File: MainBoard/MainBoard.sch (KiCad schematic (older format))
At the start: 6 parts

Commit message: add hierachy pins
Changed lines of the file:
@@
 F0 "keyboard" 50
 F1 "keyboard.sch" 50
+F2 "USB_D+" B R 10700 12500 50
+F3 "USB_D-" B R 10700 12700 50
 $EndSheet
 $EndSCHEMATC

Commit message: add hierachy pins
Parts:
- removed J?: Conn_Coaxial, symbol Connector:Conn_Coaxial
- J?: value DF40C-100DS-0.4V(51) -> DF40C-100DS-0.4V(51) _LFT
- J?: value DF40C-100DS-0.4V(51) -> DF40C-100DS-0.4V(51) _RFT
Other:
- moved on the sheet: J?
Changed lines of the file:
@@
-$EndComp
-$Comp
-L Connector:Conn_Coaxial J?
-U 1 1 60395F77
-P 21200 7000
-F 0 "J?" H 21300 6975 50  0000 L CNN
-F 1 "Conn_Coaxial" H 21300 6884 50  0000 L CNN
-F 2 "" H 21200 7000 50  0001 C CNN
-F 3 " ~" H 21200 7000 50  0001 C CNN
-	1    21200 7000
-	1    0    0    -1
 $EndComp
 $Comp
@@
 P 4850 3750
 F 0 "J?" H 4850 6417 50  0000 C CNN
-F 1 "DF40C-100DS-0.4V(51)" H 4850 6326 50  0000 C CNN
+F 1 "DF40C-100DS-0.4V(51) _LFT" H 4850 6326 50  0000 C CNN
 F 2 "HRS_DF40C-100DS-0.4V(51)" H 4850 3750 50  0001 L BNN
 F 3 "" H 4850 3750 50  0001 L BNN
@@
 L DF40C-100DS-0.4V_51_:DF40C-100DS-0.4V(51) J?
 U 1 1 6039B9F7
-P 9300 3750
-F 0 "J?" H 9300 6417 50  0000 C CNN
-F 1 "DF40C-100DS-0.4V(51)" H 9300 6326 50  0000 C CNN
-F 2 "HRS_DF40C-100DS-0.4V(51)" H 9300 3750 50  0001 L BNN
-F 3 "" H 9300 3750 50  0001 L BNN
-F 4 "HRS" H 9300 3750 50  0001 L BNN "MF"
-F 5 "None" H 9300 3750 50  0001 L BNN "PACKAGE"
-F 6 "Good" H 9300 3750 50  0001 L BNN "AVAILABILITY"
-F 7 "$1.36 USD" H 9300 3750 50  0001 L BNN "PRICE"
-F 8 "DF40C-100DS-0.4V(51)" H 9300 3750 50  0001 L BNN "MP"
-	1    9300 3750
+P 8450 3750
+F 0 "J?" H 8450 6417 50  0000 C CNN
+F 1 "DF40C-100DS-0.4V(51) _RFT" H 8450 6326 50  0000 C CNN
+F 2 "HRS_DF40C-100DS-0.4V(51)" H 8450 3750 50  0001 L BNN
+F 3 "" H 8450 3750 50  0001 L BNN
+F 4 "HRS" H 8450 3750 50  0001 L BNN "MF"
+F 5 "None" H 8450 3750 50  0001 L BNN "PACKAGE"
+F 6 "Good" H 8450 3750 50  0001 L BNN "AVAILABILITY"
+F 7 "$1.36 USD" H 8450 3750 50  0001 L BNN "PRICE"
+F 8 "DF40C-100DS-0.4V(51)" H 8450 3750 50  0001 L BNN "MP"
+	1    8450 3750
 	1    0    0    -1
 $EndComp

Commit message: add some power stuff and an extra USB port
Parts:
- added BT? (x3): _, symbol Device:Battery_Cell
- added BT?: Battery Cell, symbol Device:Battery_Cell
- added C?: 10p, symbol Device:C_Small
- added J?: USB3_A, symbol Connector:USB3_A
- added R?: 1, symbol Device:R_Small_US
- added U?: LTC4055-1, Package_DFN_QFN:QFN-16-1EP_4x4mm_P0.65mm_EP2.15x2.15mm, symbol Battery_Management:LTC4055-1
- J?: value DF40C-100DS-0.4V(51) _RFT -> DF40C-100DS-0.4V(51) _RFT (PN + 100)
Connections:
- net labels added: GND
- wire segments 0 -> 30
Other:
- moved on the sheet: J?

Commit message: switch out battery IC for better charging current
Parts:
- removed C?: 10p, symbol Device:C_Small
- removed R?: 1, symbol Device:R_Small_US
- removed U?: LTC4055-1, Package_DFN_QFN:QFN-16-1EP_4x4mm_P0.65mm_EP2.15x2.15mm, symbol Battery_Management:LTC4055-1
- added J?: Barrel_Jack, symbol Connector:Barrel_Jack
- added U?: LTC4090EDJCPBF, DFN600X300X80-23N, symbol LTC4090EDJCPBF:LTC4090EDJCPBF
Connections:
- net labels added: +5V
- wire segments 30 -> 35
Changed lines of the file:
@@
 $EndComp
-$Comp
-L Battery_Management:LTC4055-1 U?
-U 1 1 6039541B
-P 17700 9350
-F 0 "U?" H 17700 10017 50  0000 C CNN
-F 1 "LTC4055-1" H 17700 9926 50  0000 C CNN
-F 2 "Package_DFN_QFN:QFN-16-1EP_4x4mm_P0.65mm_EP2.15x2.15mm" H 17700 8450 50  0001 C CNN
-F 3 "https://www.analog.com/media/en/technical-documentation/data-sheets/4055fb.pdf" H 17700 8850 50  0001 C CNN
-	1    17700 9350
-	-1   0    0    1
-$EndComp
-Wire Wire Line
-	17300 9350 17150 9350
-Wire Wire Line
-	17150 9350 17150 9150
-Wire Wire Line
-	17150 9150 17300 9150
-Wire Wire Line
-	18100 9650 18250 9650
-Wire Wire Line
-	18250 9650 18250 8650
-Wire Wire Line
-	18250 8650 17150 8650
-Wire Wire Line
-	17150 8650 17150 9150
-Connection ~ 17150 9150
 $Comp
 L Device:Battery_Cell BT?
@@
 	16750 8400 16450 8400
 Connection ~ 16450 8400
-Wire Wire Line
-	16450 8400 16300 8400
 Connection ~ 16150 8400
 Wire Wire Line
@@
 Wire Wire Line
 	16150 8100 16300 8100
-Wire Wire Line
-	16300 8400 16300 9550
-Wire Wire Line
-	16300 9550 17300 9550
-Connection ~ 16300 8400
-Wire Wire Line
-	16300 8400 16150 8400
 $Comp
 L power:GND #PWR?
@@
 	16300 8100 16450 8100
 $Comp
-L Device:R_Small_US R?
-U 1 1 603A333E
-P 18600 9650
-F 0 "R?" H 18668 9696 50  0000 L CNN
-F 1 "1" H 18668 9605 50  0000 L CNN
-F 2 "" H 18600 9650 50  0001 C CNN
-F 3 "~" H 18600 9650 50  0001 C CNN
-	1    18600 9650
-	-1   0    0    1
-$EndComp
-$Comp
-L Device:C_Small C?
-U 1 1 603A4DA4
-P 18600 9450
-F 0 "C?" H 18692 9496 50  0000 L CNN
-F 1 "10p" H 18692 9405 50  0000 L CNN
-F 2 "" H 18600 9450 50  0001 C CNN
-F 3 "~" H 18600 9450 50  0001 C CNN
-	1    18600 9450
-	-1   0    0    1
-$EndComp
-$Comp
-L power:GND #PWR?
-U 1 1 603A62A7
-P 18600 9350
-F 0 "#PWR?" H 18600 9100 50  0001 C CNN
-F 1 "GND" H 18605 9177 50  0000 C CNN
-F 2 "" H 18600 9350 50  0001 C CNN
-F 3 "" H 18600 9350 50  0001 C CNN
-	1    18600 9350
-	-1   0    0    1
-$EndComp
-Wire Wire Line
-	18600 9750 18100 9750
-Wire Wire Line
-	20250 10000 18600 10000
-Wire Wire Line
-	18600 10000 18600 9750
-Connection ~ 18600 9750
-$Comp
 L power:GND #PWR?
 U 1 1 603AA452
@@
 	-1   0    0    1
 $EndComp
+$Comp
+L power:+5V #PWR?
+U 1 1 603ABEB6
+P 4350 5150
+F 0 "#PWR?" H 4350 5000 50  0001 C CNN
+F 1 "+5V" V 4365 5278 50  0000 L CNN
+F 2 "" H 4350 5150 50  0001 C CNN
+F 3 "" H 4350 5150 50  0001 C CNN
+	1    4350 5150
+	0    -1   -1   0
+$EndComp
+$Comp
+L power:+5V #PWR?
+U 1 1 603AC889
+P 4350 5250
+F 0 "#PWR?" H 4350 5100 50  0001 C CNN
+F 1 "+5V" V 4365 5378 50  0000 L CNN
+F 2 "" H 4350 5250 50  0001 C CNN
+F 3 "" H 4350 5250 50  0001 C CNN
+	1    4350 5250
+	0    -1   -1   0
+$EndComp
+$Comp
+L power:+5V #PWR?
+U 1 1 603AD3CB
+P 4350 5350
+F 0 "#PWR?" H 4350 5200 50  0001 C CNN
+F 1 "+5V" V 4365 5478 50  0000 L CNN
+F 2 "" H 4350 5350 50  0001 C CNN
+F 3 "" H 4350 5350 50  0001 C CNN
+	1    4350 5350
+	0    -1   -1   0
+$EndComp
+$Comp
+L power:+5V #PWR?
+U 1 1 603AD3D1
+P 4350 5450
+F 0 "#PWR?" H 4350 5300 50  0001 C CNN
+F 1 "+5V" V 4365 5578 50  0000 L CNN
+F 2 "" H 4350 5450 50  0001 C CNN
+F 3 "" H 4350 5450 50  0001 C CNN
+	1    4350 5450
+	0    -1   -1   0
+$EndComp
+$Comp
+L power:+5V #PWR?
+U 1 1 603AE08F
+P 4350 5550
+F 0 "#PWR?" H 4350 5400 50  0001 C CNN
+F 1 "+5V" V 4365 5678 50  0000 L CNN
+F 2 "" H 4350 5550 50  0001 C CNN
+F 3 "" H 4350 5550 50  0001 C CNN
+	1    4350 5550
+	0    -1   -1   0
+$EndComp
+$Comp
+L power:+5V #PWR?
+U 1 1 603AE095
+P 4350 5650
+F 0 "#PWR?" H 4350 5500 50  0001 C CNN
+F 1 "+5V" V 4365 5778 50  0000 L CNN
+F 2 "" H 4350 5650 50  0001 C CNN
+F 3 "" H 4350 5650 50  0001 C CNN
+	1    4350 5650
+	0    -1   -1   0
+$EndComp
+Wire Wire Line
+	16150 8400 16300 8400
+$Comp
+L LTC4090EDJCPBF:LTC4090EDJCPBF U?
+U 1 1 603CC1BE
+P 18200 9500
+F 0 "U?" H 18200 10570 50  0000 C CNN
+F 1 "LTC4090EDJCPBF" H 18200 10479 50  0000 C CNN
+F 2 "DFN600X300X80-23N" H 18200 9500 50  0001 L BNN
+F 3 "" H 18200 9500 50  0001 L BNN
+F 4 "LTC4090EDJC#PBF" H 18200 9500 50  0001 L BNN "MPN"
+F 5 "56M8725" H 18200 9500 50  0001 L BNN "OC_NEWARK"
+F 6 "1663728" H 18200 9500 50  0001 L BNN "OC_FARNELL"
+F 7 "Linear Technology" H 18200 9500 50  0001 L BNN "SUPPLIER"
+F 8 "DFN-16" H 18200 9500 50  0001 L BNN "PACKAGE"
+	1    18200 9500
+	1    0    0    -1
+$EndComp
+$Comp
+L Connector:Barrel_Jack J?
+U 1 1 603CD806
+P 20800 10850
+F 0 "J?" H 20570 10808 50  0000 R CNN
+F 1 "Barrel_Jack" H 20570 10899 50  0000 R CNN
+F 2 "" H 20850 10810 50  0001 C CNN
+F 3 "~" H 20850 10810 50  0001 C CNN
+	1    20800 10850
+	-1   0    0    1
+$EndComp
+$Comp
+L power:GND #PWR?
+U 1 1 603CEDD1
+P 20500 10950
+F 0 "#PWR?" H 20500 10700 50  0001 C CNN
+F 1 "GND" H 20505 10777 50  0000 C CNN
+F 2 "" H 20500 10950 50  0001 C CNN
+F 3 "" H 20500 10950 50  0001 C CNN
+	1    20500 10950
+	1    0    0    -1
+$EndComp
+Wire Wire Line
+	17400 8800 16550 8800
+Wire Wire Line
+	16550 8800 16550 11400
+Wire Wire Line
+	16550 11400 19950 11400
+Wire Wire Line
+	19950 11400 19950 10750
+Wire Wire Line
+	19950 10750 20500 10750
+Wire Wire Line
+	19000 9000 19550 9000
+$Comp
+L power:+5V #PWR?
+U 1 1 603D2A2F
+P 19550 9000
+F 0 "#PWR?" H 19550 8850 50  0001 C CNN
+F 1 "+5V" V 19565 9128 50  0000 L CNN
+F 2 "" H 19550 9000 50  0001 C CNN
+F 3 "" H 19550 9000 50  0001 C CNN
+	1    19550 9000
+	0    1    1    0
+$EndComp
+Wire Wire Line
+	17400 8900 17000 8900
+Wire Wire Line
+	17000 8900 17000 8250
+Wire Wire Line
+	17000 8250 19900 8250
+Wire Wire Line
+	19900 8250 19900 10000
+Wire Wire Line
+	19900 10000 20250 10000
+Wire Wire Line
+	19000 9300 19850 9300
+Wire Wire Line
+	19850 9300 19850 8300
+Wire Wire Line
+	19850 8300 17050 8300
+Wire Wire Line
+	17050 8300 17050 8500
+Wire Wire Line
+	17050 8500 16300 8500
+Wire Wire Line
+	16300 8500 16300 8400
+Connection ~ 16300 8400
+Wire Wire Line
+	16300 8400 16450 8400
 $EndSCHEMATC

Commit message: add key matrix and assighn footprints
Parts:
- BT1, BT2, BT3, BT4: renamed from BT?; footprint (none) -> Connector_JST:JST_PH_S2B-PH-SM4-TB_1x02-1MP_P2.00mm_Horizontal
- J1, J2: renamed from J?; footprint HRS_DF40C-100DS-0.4V(51) -> Libs:HRS_DF40C-100DS-0.4V(51)
- J3: renamed from J?; footprint (none) -> Connector_HDMI:HDMI_A_Contact_Technology_HDMI-19APL2_Horizontal
- J4: renamed from J?; footprint (none) -> Connector_BarrelJack:BarrelJack_CUI_PJ-063AH_Horizontal
- J7: renamed from J?; footprint (none) -> Connector_USB:USB_C_Receptacle_Amphenol_12401548E4-2A
- U1: renamed from U?; footprint DFN600X300X80-23N -> Libs:DFN600X300X80-23N
- gave numbers to parts that had none: 2

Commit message: move power dilevery to a hierarchy sheet and wire HDMI1
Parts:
- removed BT1: Battery Cell, Connector_JST:JST_PH_S2B-PH-SM4-TB_1x02-1MP_P2.00mm_Horizontal, symbol Device:Battery_Cell
- removed BT2, BT3, BT4: _, Connector_JST:JST_PH_S2B-PH-SM4-TB_1x02-1MP_P2.00mm_Horizontal, symbol Device:Battery_Cell
- removed U1: LTC4090EDJCPBF, Libs:DFN600X300X80-23N, symbol LTC4090EDJCPBF:LTC4090EDJCPBF
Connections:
- net +5V: now also J3.18 (+5V)
- net GND: now also J3.11 (CKS), J3.17 (GND), J3.2 (D2S), J3.5 (D1S), J3.8 (D0S), J3.SH
- net at J3.1 (D2+): now also J2.46
- net at J3.10 (CK+): now also J2.64
- net at J3.12 (CK-): now also J2.66
- net at J3.13 (CEC): now also J2.49
- net at J3.15 (SCL): now also J2.47
- net at J3.16 (SDA): now also J2.45
- net at J3.19 (HPD): now also J2.43
- net at J3.3 (D2-): now also J2.48
- net at J3.4 (D1+): now also J2.52
- net at J3.6 (D1-): now also J2.54
- net at J3.7 (D0+): now also J2.58
- net at J3.9 (D0-): now also J2.60
- net Power_Delivery/5v_IN: now reaches J7.A4 (VBUS), J7.A9 (VBUS), J7.B4 (VBUS), J7.B9 (VBUS)
- net at J7.A5 (CC1): now also J1.96
- net at J7.B5 (CC2): now also J1.94
- net Power_Delivery/HV_IN: now reaches J4.2
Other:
- moved on the sheet: J3, J5, J6

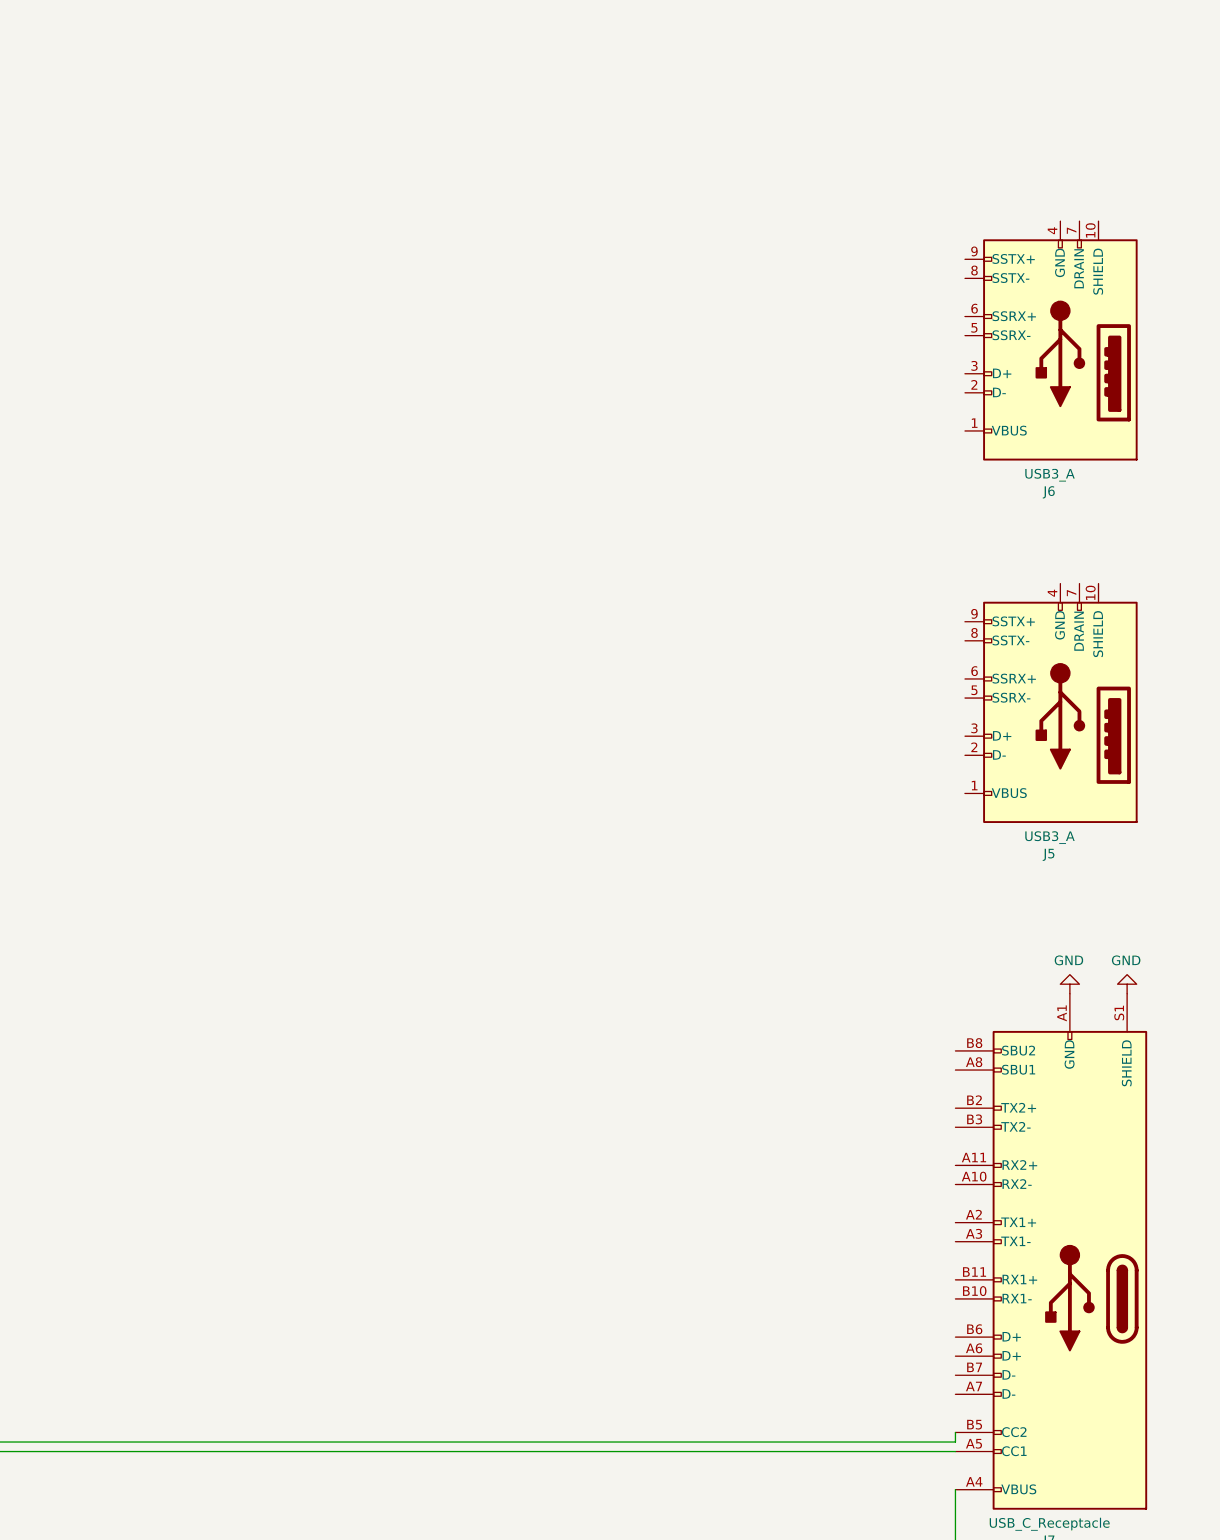
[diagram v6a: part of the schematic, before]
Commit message: Add usb 3 chip in hierarchy sheet and wire ports
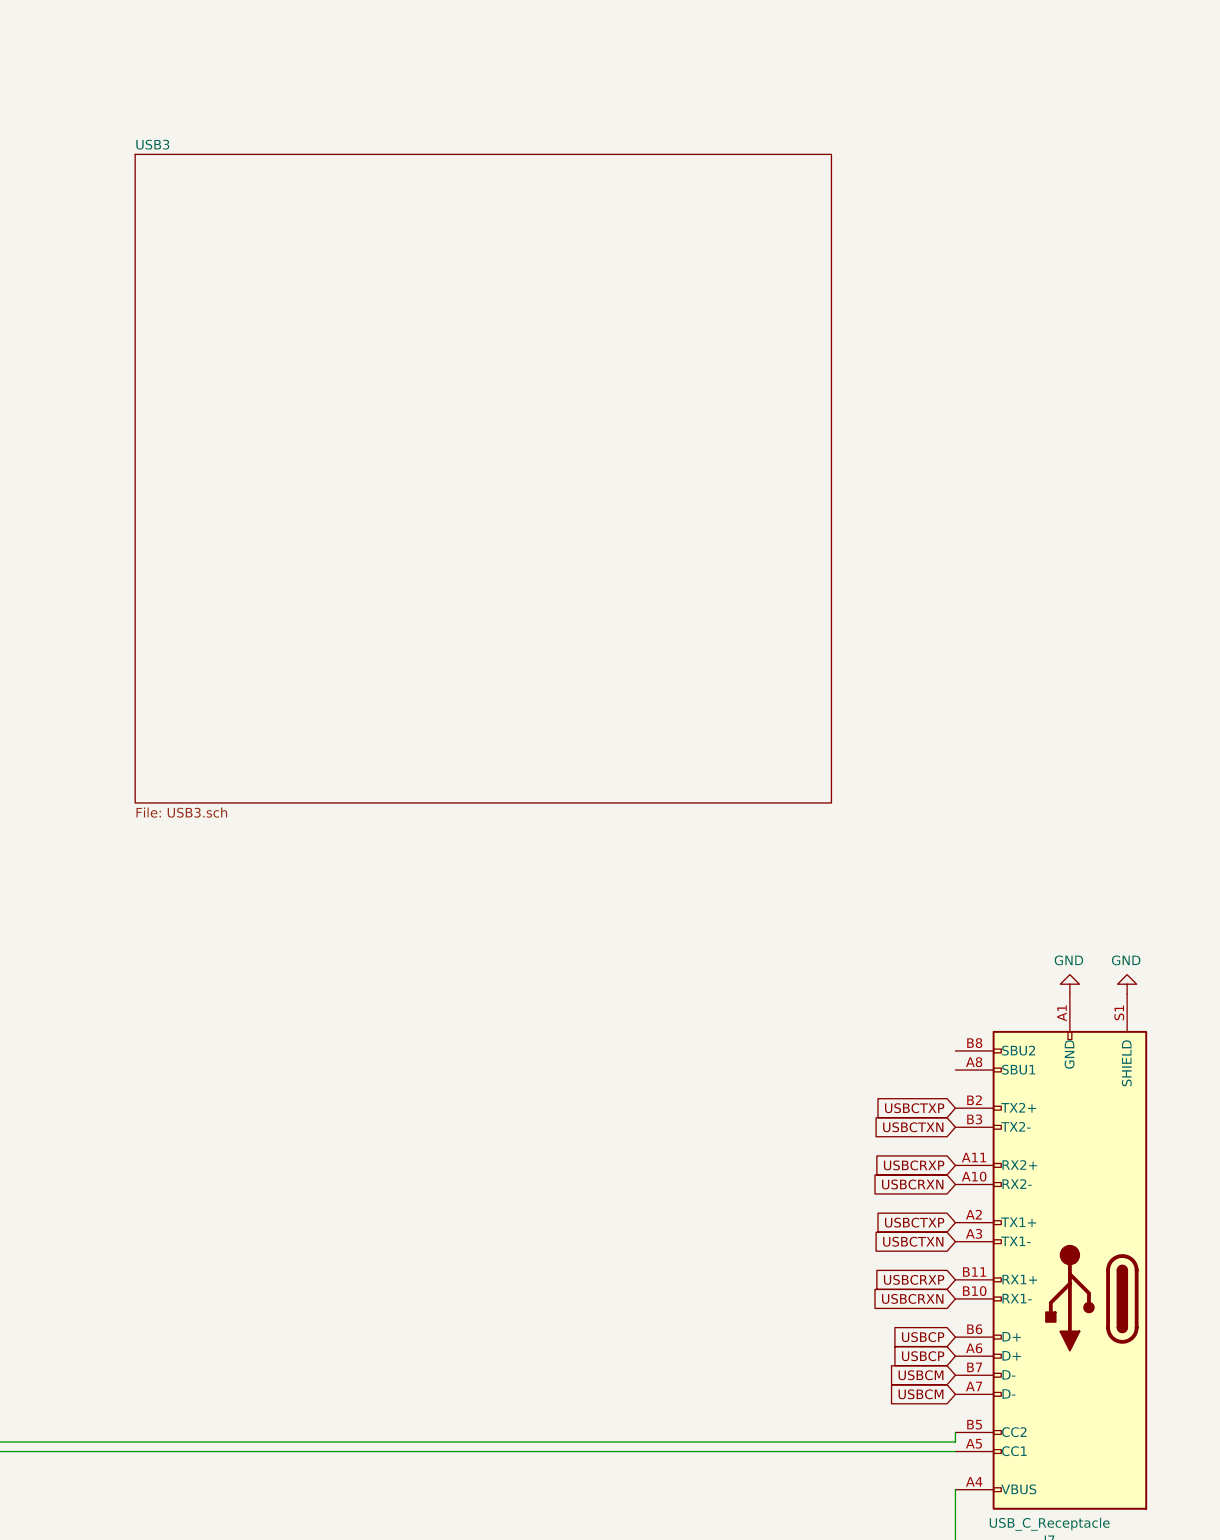
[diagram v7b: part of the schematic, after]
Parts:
- removed J5, J6: USB3_A, symbol Connector:USB3_A
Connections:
- net USBCRXN: now reaches J7.A10 (RX2-)
- net USBCRXN: now also J7.B10 (RX1-)
- net USBCRXP: now reaches J7.A11 (RX2+)
- net USBCRXP: now also J7.B11 (RX1+)
- net USBCTXP: now reaches J7.A2 (TX1+)
- net USBCTXP: now also J7.B2 (TX2+)
- net USBCTXN: now reaches J7.A3 (TX1-)
- net USBCTXN: now also J7.B3 (TX2-)
- net USBCP: now reaches J7.A6 (D+)
- net USBCP: now also J7.B6 (D+)
- net USBCM: now reaches J7.A7 (D-)
- net USBCM: now also J7.B7 (D-)
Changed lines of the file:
@@
 $Descr A2 23386 16535
 encoding utf-8
-Sheet 1 3
+Sheet 1 4
 Title ""
 Date ""
@@
 	1    12150 3800
 	1    0    0    -1
-$EndComp
-$Comp
-L Connector:USB3_A J5
-U 1 1 6038114B
-P 20800 5950
-F 0 "J5" H 20857 6667 50  0000 C CNN
-F 1 "USB3_A" H 20857 6576 50  0000 C CNN
-F 2 "" H 20950 6050 50  0001 C CNN
-F 3 "~" H 20950 6050 50  0001 C CNN
-	1    20800 5950
-	-1   0    0    1
 $EndComp
 $Comp
@@
 	11050 12500 10700 12500
 $Comp
-L Connector:USB3_A J6
-U 1 1 603DA7EB
-P 20800 4050
-F 0 "J6" H 20857 4767 50  0000 C CNN
-F 1 "USB3_A" H 20857 4676 50  0000 C CNN
-F 2 "" H 20950 4150 50  0001 C CNN
-F 3 "~" H 20950 4150 50  0001 C CNN
-	1    20800 4050
-	-1   0    0    1
-$EndComp
-$Comp
 L power:GND #PWR057
 U 1 1 603AA452
@@
 	20250 11150 20250 10000
 $Comp
-L power:+5V #PWR?
+L power:+5V #PWR0101
 U 1 1 603B66DB
 P 18700 11000
-F 0 "#PWR?" H 18700 10850 50  0001 C CNN
+F 0 "#PWR0101" H 18700 10850 50  0001 C CNN
 F 1 "+5V" V 18715 11128 50  0000 L CNN
 F 2 "" H 18700 11000 50  0001 C CNN
@@
 	6700 3450 7950 3450
 $Comp
-L power:GND #PWR?
+L power:GND #PWR0102
 U 1 1 6041E9A9
 P 11950 4900
-F 0 "#PWR?" H 11950 4650 50  0001 C CNN
+F 0 "#PWR0102" H 11950 4650 50  0001 C CNN
 F 1 "GND" H 11955 4727 50  0000 C CNN
 F 2 "" H 11950 4900 50  0001 C CNN
@@
 $EndComp
 $Comp
-L power:GND #PWR?
+L power:GND #PWR0103
 U 1 1 6041F062
 P 12050 4900
-F 0 "#PWR?" H 12050 4650 50  0001 C CNN
+F 0 "#PWR0103" H 12050 4650 50  0001 C CNN
 F 1 "GND" H 12055 4727 50  0000 C CNN
 F 2 "" H 12050 4900 50  0001 C CNN
@@
 $EndComp
 $Comp
-L power:GND #PWR?
+L power:GND #PWR0104
 U 1 1 6041F618
 P 12150 4900
-F 0 "#PWR?" H 12150 4650 50  0001 C CNN
+F 0 "#PWR0104" H 12150 4650 50  0001 C CNN
 F 1 "GND" H 12155 4727 50  0000 C CNN
 F 2 "" H 12150 4900 50  0001 C CNN
@@
 $EndComp
 $Comp
-L power:GND #PWR?
+L power:GND #PWR0105
 U 1 1 604210C0
 P 12250 4900
-F 0 "#PWR?" H 12250 4650 50  0001 C CNN
+F 0 "#PWR0105" H 12250 4650 50  0001 C CNN
 F 1 "GND" H 12255 4727 50  0000 C CNN
 F 2 "" H 12250 4900 50  0001 C CNN
@@
 $EndComp
 $Comp
-L power:GND #PWR?
+L power:GND #PWR0106
 U 1 1 60422AF8
 P 12350 4900
-F 0 "#PWR?" H 12350 4650 50  0001 C CNN
+F 0 "#PWR0106" H 12350 4650 50  0001 C CNN
 F 1 "GND" H 12355 4727 50  0000 C CNN
 F 2 "" H 12350 4900 50  0001 C CNN
@@
 $EndComp
 $Comp
-L power:GND #PWR?
+L power:GND #PWR0107
 U 1 1 6042452A
 P 12450 4900
-F 0 "#PWR?" H 12450 4650 50  0001 C CNN
+F 0 "#PWR0107" H 12450 4650 50  0001 C CNN
 F 1 "GND" H 12455 4727 50  0000 C CNN
 F 2 "" H 12450 4900 50  0001 C CNN
@@
 $EndComp
 $Comp
-L power:+5V #PWR?
+L power:+5V #PWR0108
 U 1 1 60426A75
 P 12150 2700
-F 0 "#PWR?" H 12150 2550 50  0001 C CNN
+F 0 "#PWR0108" H 12150 2550 50  0001 C CNN
 F 1 "+5V" H 12165 2873 50  0000 C CNN
 F 2 "" H 12150 2700 50  0001 C CNN
@@
 	1    0    0    -1
 $EndComp
+$Sheet
+S 15950 3000 3650 3400
+U 6042C255
+F0 "USB3" 50
+F1 "USB3.sch" 50
+$EndSheet
+Text GLabel 20250 8000 0    50   Input ~ 0
+USBCTXP
+Text GLabel 20250 8600 0    50   Input ~ 0
+USBCTXP
+Text GLabel 20250 8100 0    50   Input ~ 0
+USBCTXN
+Text GLabel 20250 8700 0    50   Input ~ 0
+USBCTXN
+Text GLabel 20250 8300 0    50   Input ~ 0
+USBCRXP
+Text GLabel 20250 8900 0    50   Input ~ 0
+USBCRXP
+Text GLabel 20250 8400 0    50   Input ~ 0
+USBCRXN
+Text GLabel 20250 9000 0    50   Input ~ 0
+USBCRXN
+Text GLabel 20250 9200 0    50   Input ~ 0
+USBCP
+Text GLabel 20250 9300 0    50   Input ~ 0
+USBCP
+Text GLabel 20250 9400 0    50   Input ~ 0
+USBCM
+Text GLabel 20250 9500 0    50   Input ~ 0
+USBCM
 $EndSCHEMATC
